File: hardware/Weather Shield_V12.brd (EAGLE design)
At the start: 53.3 x 59.7 mm, 48 parts, among them J1 GP-635T, Q1 BSS138, Q2 BSS138, U1 ARDUINO_R3_SHIELD, U2 3.3V MIC5219, U3 ALS-PT19, U4 MPL3115A2LGA8, U5 HTU21D

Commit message: V1.2 Initial Checklist pushes
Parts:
- removed U5: HTU21D, SparkFun-Sensors:HTU21D
- added FD1, FD2: FIDUCIAL1X2, SparkFun-Aesthetics:FIDUCIAL-1X2
- added U$1: SI7021, SparkFun-Sensors:SI7021
- added U$2: REVISION, SparkFun-Aesthetics:REVISION
- S2: value Serial Select -> DPDT
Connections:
- net 3.3V: now also U$1.VDD; no longer U5.VDD
- net GND: now also U$1.GND; no longer U5.7, U5.GND
- net SCL: now also U$1.SCK; no longer U5.SCK
- net SDA: now also U$1.DATA; no longer U5.DATA
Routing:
- net GND: track 44.7 -> 46.4 mm
- net GRXI: track 39.8 -> 40.7 mm
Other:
- outline, holes or cut-outs redrawn
- board text added: "Joel Bartlett"
- board text added: "Route Out"
- board text added: "Temp & Humidity"
- board text added: "v12"
- board text removed: "Humidity"
- board text removed: "v11"

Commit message: Fixed 4-way junctions
Fixed 4-way junctions
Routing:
- net WDIR: track 15.6 -> 13.0 mm
- net RAIN: track 30.7 -> 28.3 mm
- net WSPEED: track 45.6 -> 43.3 mm
- net BATT_LVL: track 55.7 -> 54.4 mm
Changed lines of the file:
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@@
 <layer number="47" name="Measures" color="7" fill="1" visible="no" active="yes"/>
 <layer number="48" name="Document" color="7" fill="1" visible="no" active="yes"/>
-<layer number="49" name="Reference" color="7" fill="1" visible="yes" active="yes"/>
+<layer number="49" name="Reference" color="7" fill="1" visible="no" active="yes"/>
 <layer number="50" name="dxf" color="7" fill="1" visible="no" active="yes"/>
 <layer number="51" name="tDocu" color="6" fill="1" visible="yes" active="yes"/>
@@
 <layer number="112" name="tSilk" color="7" fill="1" visible="no" active="yes"/>
 <layer number="113" name="IDFDebug" color="7" fill="1" visible="no" active="yes"/>
-<layer number="114" name="Badge_Outline" color="7" fill="1" visible="yes" active="yes"/>
-<layer number="115" name="ReferenceISLANDS" color="7" fill="1" visible="yes" active="yes"/>
+<layer number="114" name="Badge_Outline" color="7" fill="1" visible="no" active="yes"/>
+<layer number="115" name="ReferenceISLANDS" color="7" fill="1" visible="no" active="yes"/>
 <layer number="116" name="Patch_BOT" color="9" fill="4" visible="no" active="yes"/>
 <layer number="118" name="Rect_Pads" color="7" fill="1" visible="no" active="yes"/>
@@
 <signal name="RAIN">
 <contactref element="R11" pad="1"/>
-<contactref element="D6" pad="1"/>
 <contactref element="D5" pad="2"/>
 <contactref element="U1" pad="D2"/>
@@
 <wire x1="14.82" y1="38.95" x2="13.97" y2="38.1" width="0.254" layer="1"/>
 <wire x1="13.97" y1="38.1" x2="7.62" y2="38.1" width="0.254" layer="1"/>
-<wire x1="20.44" y1="39.37" x2="18.93" y2="39.37" width="0.254" layer="1"/>
-<wire x1="18.93" y1="39.37" x2="18.93" y2="40.252" width="0.254" layer="1"/>
 <wire x1="18.93" y1="40.252" x2="18.542" y2="40.64" width="0.254" layer="1"/>
 <wire x1="18.542" y1="40.64" x2="15.24" y2="40.64" width="0.254" layer="1"/>
+<contactref element="D6" pad="1"/>
+<wire x1="18.93" y1="39.37" x2="20.44" y2="39.37" width="0" layer="19" extent="1-1"/>
+<wire x1="18.93" y1="40.252" x2="18.93" y2="39.37" width="0" layer="19" extent="1-1"/>
 </signal>
 <signal name="WSPEED">
 <contactref element="R14" pad="1"/>
 <contactref element="D9" pad="2"/>
-<contactref element="D10" pad="1"/>
 <contactref element="U1" pad="D3"/>
 <wire x1="2.54" y1="46.99" x2="3.81" y2="46.99" width="0.254" layer="1"/>
@@
 <wire x1="32.9" y1="36.83" x2="32.9" y2="36.075" width="0.254" layer="1"/>
 <wire x1="32.9" y1="36.075" x2="32.385" y2="35.56" width="0.254" layer="1"/>
-<wire x1="34.41" y1="36.83" x2="32.9" y2="36.83" width="0.254" layer="1"/>
-<wire x1="34.41" y1="36.83" x2="34.41" y2="37.585" width="0.254" layer="1"/>
 <wire x1="34.41" y1="37.585" x2="34.925" y2="38.1" width="0.254" layer="1"/>
 <wire x1="35.98" y1="39.37" x2="35.98" y2="38.52" width="0.254" layer="1"/>
 <wire x1="35.98" y1="38.52" x2="35.56" y2="38.1" width="0.254" layer="1"/>
 <wire x1="35.56" y1="38.1" x2="34.925" y2="38.1" width="0.254" layer="1"/>
+<contactref element="D10" pad="1"/>
+<wire x1="34.41" y1="36.83" x2="34.41" y2="37.585" width="0" layer="19" extent="1-1"/>
+<wire x1="32.9" y1="36.83" x2="34.41" y2="36.83" width="0" layer="19" extent="1-1"/>
 </signal>
 <signal name="WDIR">
 <contactref element="R17" pad="2"/>
 <contactref element="R13" pad="1"/>
-<contactref element="D8" pad="1"/>
 <contactref element="D7" pad="2"/>
 <contactref element="U1" pad="A0"/>
-<wire x1="40.52" y1="36.83" x2="42.03" y2="36.83" width="0.254" layer="1"/>
 <wire x1="41.49" y1="39.37" x2="41.49" y2="38.52" width="0.254" layer="1"/>
 <wire x1="41.49" y1="38.52" x2="42.03" y2="37.98" width="0.254" layer="1"/>
-<wire x1="42.03" y1="36.83" x2="42.03" y2="37.98" width="0.254" layer="1"/>
 <wire x1="43.6" y1="39.37" x2="41.49" y2="39.37" width="0.254" layer="1"/>
 <wire x1="43.6" y1="39.37" x2="43.6" y2="41.06" width="0.254" layer="1"/>
 <wire x1="43.6" y1="41.06" x2="44.45" y2="41.91" width="0.254" layer="1"/>
 <wire x1="44.45" y1="41.91" x2="50.8" y2="41.91" width="0.254" layer="1"/>
+<contactref element="D8" pad="1"/>
+<wire x1="42.03" y1="36.83" x2="42.03" y2="37.98" width="0" layer="19" extent="1-1"/>
+<wire x1="40.52" y1="36.83" x2="42.03" y2="36.83" width="0" layer="19" extent="1-1"/>
 </signal>
 <signal name="RAIN2">
@@
 <signal name="BATT_LVL">
 <contactref element="R8" pad="2"/>
-<contactref element="R7" pad="1"/>
 <contactref element="U1" pad="A2"/>
 <wire x1="50.8" y1="46.99" x2="52.07" y2="45.72" width="0.254" layer="16"/>
@@
 <via x="30.48" y="16.51" extent="1-16" drill="0.508"/>
 <wire x1="30.48" y1="16.51" x2="30.48" y2="18.2" width="0.254" layer="1"/>
-<wire x1="30.48" y1="18.2" x2="31.75" y2="18.2" width="0.254" layer="1"/>
 <wire x1="30.48" y1="18.2" x2="29.21" y2="18.2" width="0.254" layer="1"/>
 <wire x1="52.07" y1="18.415" x2="51.435" y2="17.78" width="0.254" layer="16"/>
 <wire x1="51.435" y1="17.78" x2="49.53" y2="17.78" width="0.254" layer="16"/>
 <wire x1="49.53" y1="17.78" x2="48.26" y2="16.51" width="0.254" layer="16"/>
+<contactref element="R7" pad="1"/>
+<wire x1="30.48" y1="18.2" x2="31.75" y2="18.2" width="0" layer="19" extent="1-1"/>
 </signal>
 <signal name="3V_PWR_CTL">

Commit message: Post group review changes
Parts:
- added JP1: (no value), SparkFun-Passives:PAD-JUMPER-2-NC_BY_TRACE_NO_SILK
- moved FD2 76.3 mm to (3.81, 57.1)
- moved FD1 7.62 mm to (49.5, 5.08)
- renumbered U$1 to U5
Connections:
- net RAW renamed VIN
- new net N$6: JP1.1, U1.D12
- net INT-PRESSURE: now also JP1.2
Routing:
- net INT-PRESSURE: track 0.00 -> 36.4 mm, vias 0 -> 2
- net STAT2: track 7.59 -> 2.01 mm
- net N$6: track 0.00 -> 3.83 mm
- net WDIR: track 13.0 -> 15.6 mm
- net STAT1: track 13.4 -> 10.9 mm
- net RAIN: track 28.3 -> 30.7 mm
- net WSPEED: track 43.3 -> 45.6 mm
- net BATT_LVL: track 54.4 -> 55.7 mm
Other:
- board text added: "3.3V"
- board text added: "A1"
- board text added: "Batt Lvl"
- board text added: "D7"
- board text added: "D8"
- board text added: "GPS PWR"
- board text added: "GRX"
- board text added: "GTX"
- board text added: "INT_P"
- board text added: "LED1"
- board text added: "LED2"
- board text added: "RAIN"
- board text added: "SCL"
- board text added: "SDA"
- board text added: "STAT LEDS"
- board text added: "WDir"
- board text added: "WSpd"
- board text removed: "Status"

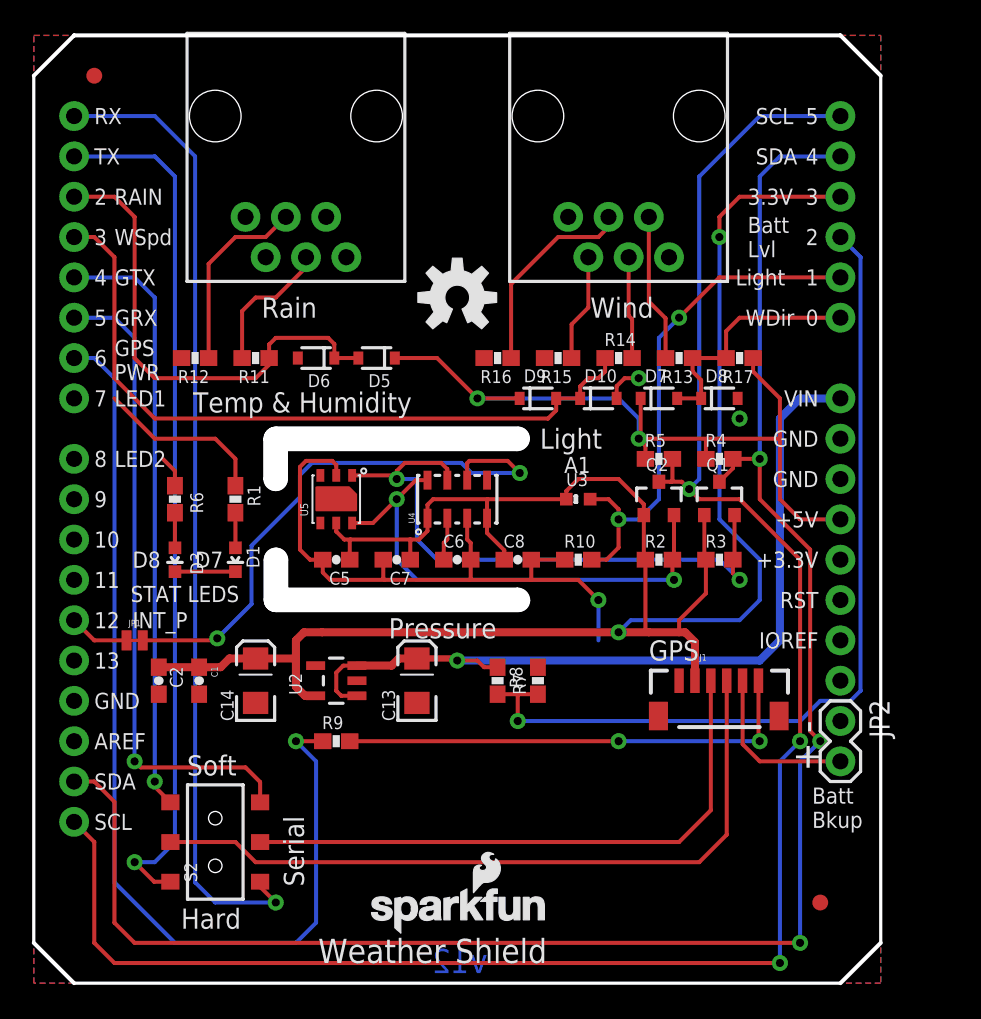
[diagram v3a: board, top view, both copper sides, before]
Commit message: Post QC Checklist fixes
Addressed the few issues that came up during the preliminary QC
checklist. Mostly PROD_IDs missing and aesthetic fixes.
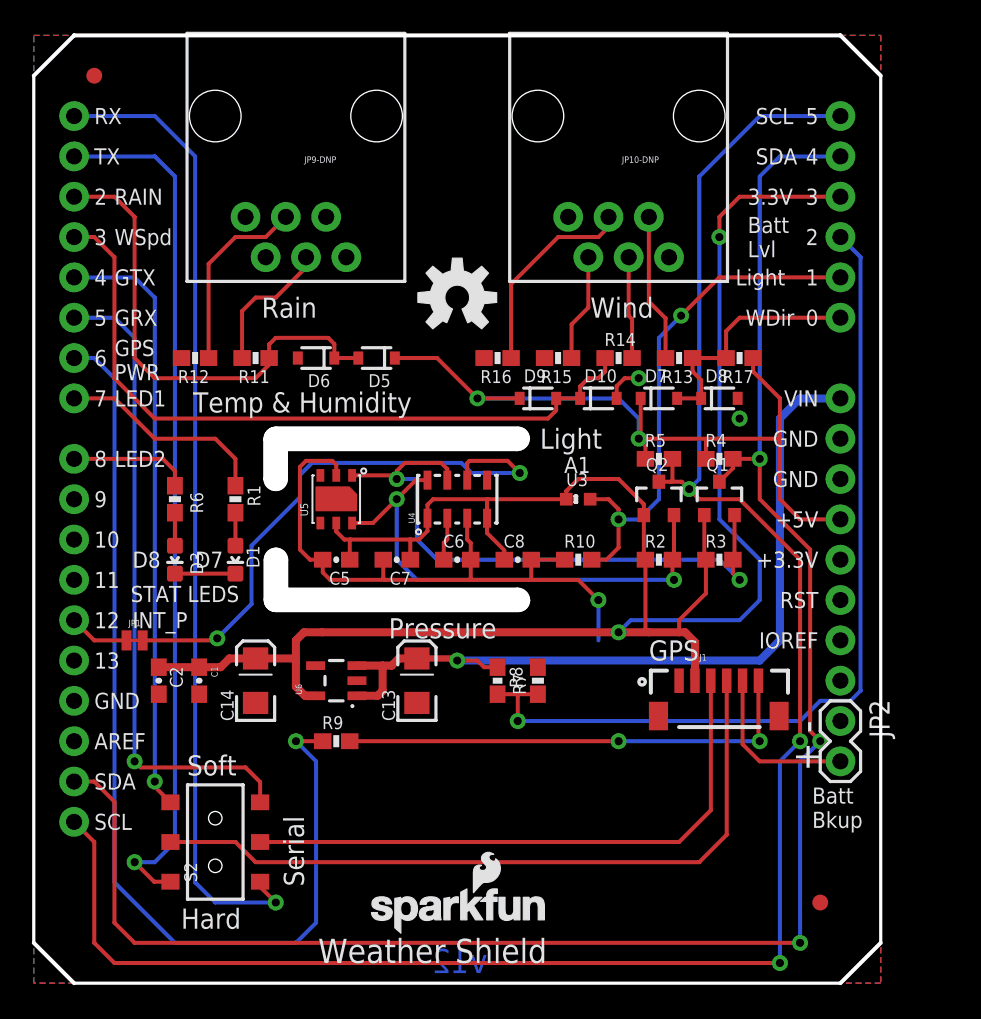
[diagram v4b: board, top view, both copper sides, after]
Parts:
- removed U2: 3.3V MIC5219, SparkFun:SOT23-5
- added U6: 3.3V/150mA, SparkFun-PowerIC:SOT23-5
- C1, C8: value 1uF -> 1.0uF; device SparkFun:0603-CAP -> SparkFun-Capacitors:0603-CAP
- C13, C14: device SparkFun-Passives:EIA3216 -> SparkFun-Capacitors:EIA3216
- C2, C5, C6, C7: device SparkFun:0603-CAP -> SparkFun-Capacitors:0603-CAP
- D1: value Blue -> BLUE; device SparkFun:LED-0603 -> SparkFun-LED:LED-0603
- D10, D5, D6, D7, D8, D9: value BAS16 -> 250mA/100V; device SparkFun:SOD-323 -> SparkFun-DiscreteSemi:SOD-323
- D3: value Green -> GREEN; device SparkFun:LED-0603 -> SparkFun-LED:LED-0603
- J1: value GP-635T -> GP-735
- JP10-DNP, JP9-DNP: device SparkFun:RJ11-6 -> SparkFun-Connectors:RJ11-6
- Q1, Q2: value BSS138 -> 200mA/50V; device SparkFun:SOT23-3 -> SparkFun-DiscreteSemi:SOT23-3
- R1, R11, R12, R13, R14, R15, R16, R17, R2, R3, R4, R5, R6, R7, R9: device SparkFun:0603-RES -> SparkFun-Resistors:0603-RES
- R10: device SparkFun-Passives:0603-RES -> SparkFun-Resistors:0603-RES
- R8: device SparkFun:0603-RES -> SparkFun-Resistors:0603
- moved JP10-DNP 5.08 mm to (36.8, 54.6)
- moved JP9-DNP 5.08 mm to (16.5, 54.6)
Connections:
- net 3.3V: now also U6.5; no longer U2.5
- net 5V: now also D5.C, D7.C, D9.C; no longer D5.1, D7.1, D9.1
- net GND: now also D10.A, D6.A, D8.A, U6.2; no longer D10.2, D6.2, D8.2, U2.2
- net RAIN: now also D5.A, D6.C; no longer D5.2, D6.1
- net VIN: now also U6.1, U6.3; no longer U2.1, U2.3
- net WDIR: now also D7.A, D8.C; no longer D7.2, D8.1
- net WSPEED: now also D10.C, D9.A; no longer D10.1, D9.2
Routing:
- net STAT2: track 2.01 -> 7.59 mm
- net STAT1: track 10.9 -> 13.4 mm
- net VIN: track 52.5 -> 51.8 mm
